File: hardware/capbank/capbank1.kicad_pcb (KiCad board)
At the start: 2 copper layers, 99 x 70.5 mm, 116 parts, among them J1 Screws, J3 Conn_01x02, J4 Conn_01x02, J5 Conn_01x06, K1 3570.1333.121 COMUS, K2 3570.1333.121 COMUS, K4 3570.1333.121 COMUS, SW2 SW_SPST, U1 ULN2003, U10 TS861IL, U11 NXJ1S1212MC, U12 LM317AEMP, U13 74HC14, U14 MCP1415, U15 MCP1415, U16 LM78L05ACZ, U2 OPA2202IDR, U3 MCP1525-TO, U4 MCP4921-EP, U5 PAI130M61, U6 ATtiny84A-P, U7 4046, U9 LM78L05ACZ, Y1 16MHz

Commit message: Small hardware changes
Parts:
- removed C18: 100n, PCM_Capacitor_SMD_AKL:C_0603_1608Metric
- removed C26, C49: 10u, PCM_Capacitor_THT_AKL:CP_Radial_D5.0mm_P2.00mm
- removed TP1, TP10, TP2, TP3, TP4, TP9: ~, TestPoint:TestPoint_THTPad_1.5x1.5mm_Drill0.7mm
- removed U6: ATtiny84A-P, Package_DIP:DIP-14_W7.62mm
- added C1: 100n, PCM_Capacitor_SMD_AKL:C_0603_1608Metric, F.Cu at (101.0, 100.0)
- added U8: ATtiny84A-SS, Package_SO:SOIC-14_3.9x8.7mm_P1.27mm, F.Cu at (131.5, 58.3)
- D4, D5, D6: value 1N5711 -> BAT46WJ; footprint Diode_THT:D_DO-35_SOD27_P7.62mm_Horizontal -> PCM_Diode_SMD_AKL:D_SOD-323
- D7: value 1N4007 -> 1N4007W; footprint Diode_THT:D_DO-35_SOD27_P7.62mm_Horizontal -> PCM_Diode_SMD_AKL:D_SOD-123
- U7: value 4046 -> 74HC4046AD; footprint Package_DIP:DIP-16_W7.62mm -> Package_SO:SOIC-16_3.9x9.9mm_P1.27mm
- Y1: footprint Crystal:Resonator-3Pin_W7.0mm_H2.5mm -> PCM_Crystal_Handsoldering_AKL:Resonator_SMD_muRata_CSTxExxV-3Pin_3.0x1.1mm_BigPads
- moved JP8 47.5 mm to (131.4, 52.4)
- moved C41 40.9 mm to (128.7, 70.2), turned to -90 degrees
- moved C46 40.5 mm to (115.5, 100.4)
- moved C48 40.1 mm to (102.7, 74.7), turned to 180 degrees
- moved D4 39.3 mm to (126.1, 107.4), turned to 90 degrees
- moved D5 39.2 mm to (125.3, 104.3)
- moved D6 39.1 mm to (126.1, 101.4), turned to -90 degrees
- moved C13 39.0 mm to (114.0, 92.2), turned to -90 degrees
- moved J4 38.2 mm to (116.6, 66.5)
- moved R16 38.1 mm to (127.0, 70.2), turned to 90 degrees
- moved C45 37.9 mm to (133.5, 98.8), turned to 0 degrees
- moved C20 37.8 mm to (117.0, 100.4), turned to -90 degrees
- moved H1 37.4 mm to (162.0, 92.0)
- moved C19 36.3 mm to (116.9, 106.3)
- moved C47 36.3 mm to (115.4, 106.3)
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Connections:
- J1 pad 1: GND -> V_SUPPLY
- J1 pad 2: V_SUPPLY -> GND
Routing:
- net V_SUPPLY: track 213.2 -> 167.4 mm, vias 3 -> 1
- net /Isolated/VTUNE: track 15.8 -> 61.4 mm, vias 0 -> 2
- net VDD: track 201.5 -> 156.9 mm, vias 4 -> 0
- net GND_ISOL: track 100.1 -> 140.6 mm, vias 17 -> 31
- net /Microcontroller/HVSP_CLK_FSK_IN: track 48.4 -> 9.27 mm, vias 6 -> 0
- net /Microcontroller/PRG_MOSI_I2C_SDA: track 39.5 -> 4.67 mm
- net /Microcontroller/FSK_DEMOD: track 4.53 -> 35.9 mm, vias 0 -> 4
- net /SCK: track 17.1 -> 38.2 mm, vias 0 -> 2
- net /Microcontroller/~{RESET}: track 31.4 -> 10.7 mm
- net /SDI: track 16.6 -> 34.9 mm
- net /Microcontroller/PRG_SCK_I2C_SCL: track 25.3 -> 7.00 mm
- net VDD_ISOL: track 84.5 -> 100.0 mm, vias 2 -> 1
- net HV_CLEAN: track 52.6 -> 67.9 mm, vias 2 -> 1
- net /Microcontroller/FSK Demod/FSK_DEMOD: track 5.53 -> 20.4 mm, vias 0 -> 2
- net V_SUPPLY_ISOL: track 28.9 -> 39.7 mm
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- added copper zone on F.Cu, net /Isolated/ANT1
- added copper zone on F.Cu, net /Isolated/ANT2
- added copper zone on F.Cu, net GND
- added copper zone on F.Cu, net GND_ISOL
- added copper zone on F.Cu, net Net-(D1-K)
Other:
- board size 99 x 70.5 mm -> 91 x 64 mm
- board text added: "+"
- board text added: "GND"
- board text added: "MISO"
- board text added: "MOSI"
- board text added: "SCK"
- board text added: "VDD"
- board text added: "Varactor Board Rev A"
- board text added: "contact@tatjam.eu"
- board text added: "~{RST}"
- board text added: "▲"

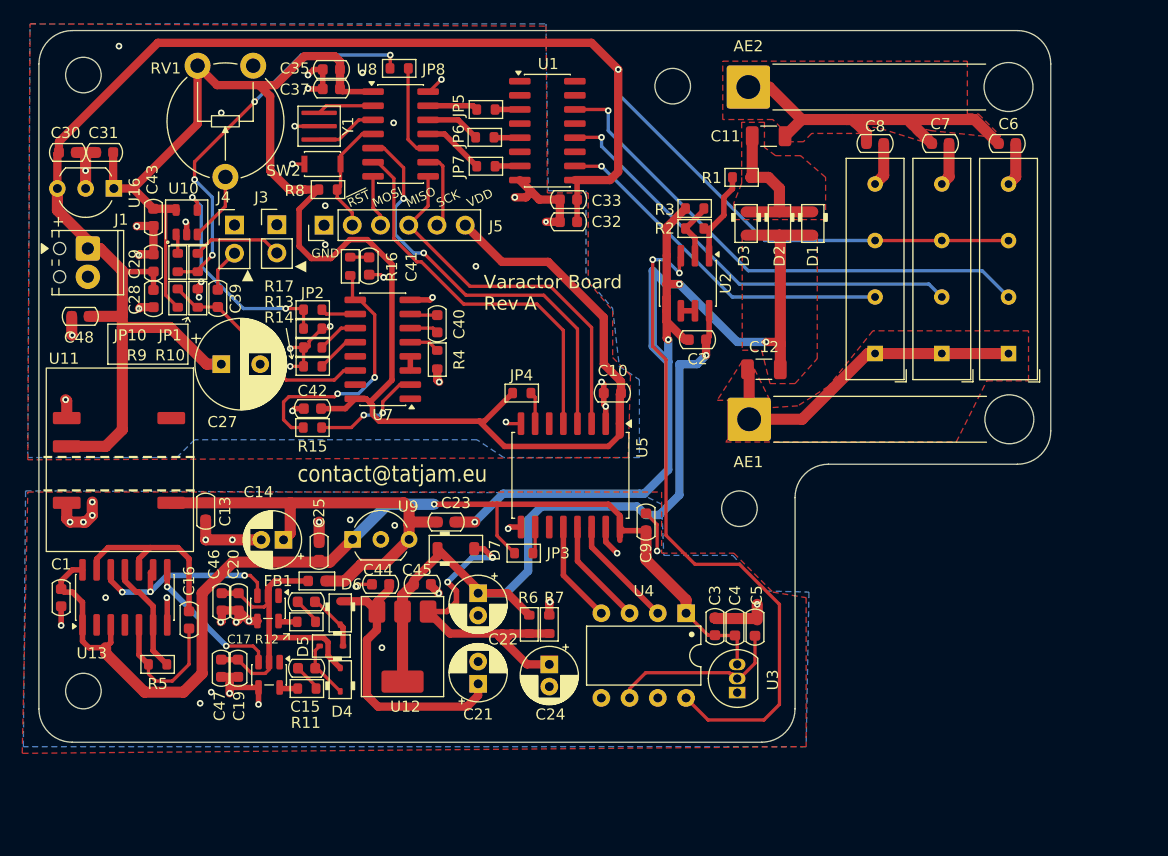
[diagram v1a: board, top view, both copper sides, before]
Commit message: Add footprint for buffered-filter and replace pot with digital pot
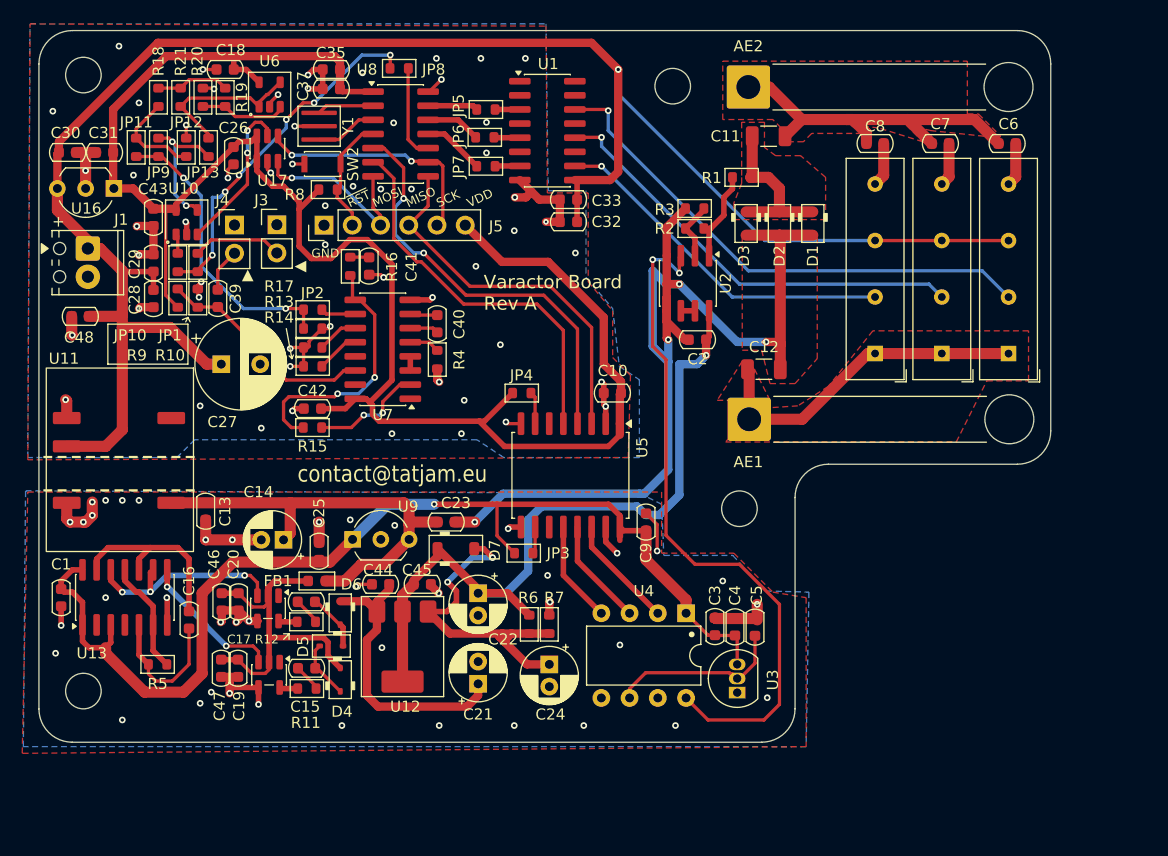
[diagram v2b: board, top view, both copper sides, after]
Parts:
- removed RV1: 10k, PCM_Potentiometer_THT_AKL:Potentiometer_Piher_PT-10-V10_Vertical
- added C18: 100n, PCM_Capacitor_SMD_AKL:C_0603_1608Metric, F.Cu at (115.8, 52.5)
- added C26: 100n, PCM_Capacitor_SMD_AKL:C_0603_1608Metric, F.Cu at (116.5, 60.2)
- added JP11: 0, PCM_Resistor_SMD_AKL:R_0603_1608Metric, F.Cu at (107.8, 59.5)
- added JP12: 0, PCM_Resistor_SMD_AKL:R_0603_1608Metric, F.Cu at (112.2, 59.5)
- added JP13: 0, PCM_Resistor_SMD_AKL:R_0603_1608Metric, F.Cu at (114.2, 59.5)
- added JP9: 0, PCM_Resistor_SMD_AKL:R_0603_1608Metric, F.Cu at (109.8, 59.5)
- added R18: 10k, PCM_Resistor_SMD_AKL:R_0603_1608Metric, F.Cu at (109.8, 55.0)
- added R19: 10k, PCM_Resistor_SMD_AKL:R_0603_1608Metric, F.Cu at (115.8, 55.0)
- added R20: 10k, PCM_Resistor_SMD_AKL:R_0603_1608Metric, F.Cu at (113.8, 55.0)
- added R21: 10k, PCM_Resistor_SMD_AKL:R_0603_1608Metric, F.Cu at (111.8, 55.0)
- added U17: MCP4012-xxxxCH, Package_TO_SOT_SMD:SOT-23-6, F.Cu at (119.5, 59.6)
- added U6: MCP6021T-E-OT, PCM_Package_TO_SOT_SMD_AKL:SOT-23-5, F.Cu at (119.8, 54.8)
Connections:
- net /Microcontroller/PRG_MOSI_I2C_SDA renamed /Microcontroller/PRG_MOSI_RHEO_UD
- net /Microcontroller/PRG_SCK_I2C_SCL renamed /Microcontroller/PRG_SCK_RHEO_CS
- net Net-(D4-A) renamed /BiasSupply/SWITCH_SUPPLY
- net Net-(U2A--) renamed /Isolated/Varactor/VBIAS_FB
- U10 pad 4: /Microcontroller/FSK Demod/FSK_DEMOD -> /Microcontroller/FSK Demod/FSK_FILT
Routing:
- net /Microcontroller/PRG_SCK_RHEO_CS: track 7.00 -> 21.8 mm, vias 0 -> 2
- net Net-(JP13-A): track 0.00 -> 14.6 mm
- net /Microcontroller/FSK Demod/FSK_FILT: track 0.00 -> 12.6 mm, vias 0 -> 2
- net /Microcontroller/PRG_MOSI_RHEO_UD: track 4.67 -> 17.0 mm, vias 0 -> 1
- net Net-(JP11-B): track 0.00 -> 8.86 mm
- net VDD: track 156.9 -> 165.0 mm
- net Net-(U10-+): track 6.22 -> 14.2 mm, vias 0 -> 2
- net Net-(U6-+): track 0.00 -> 7.87 mm
- net GND: track 55.5 -> 63.0 mm, vias 33 -> 57
- net Net-(R18-Pad2): track 0.00 -> 6.62 mm
- net /Microcontroller/FSK Demod/FSK_DEMOD: track 20.4 -> 26.2 mm
- net /Microcontroller/FSK_DEMOD: track 35.9 -> 32.1 mm, vias 4 -> 6
- net GND_ISOL: vias 31 -> 45

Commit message: Update PCB with learned lessons
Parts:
- added C34: 100n, PCM_Capacitor_SMD_AKL:C_0603_1608Metric, F.Cu at (123.5, 86.5)
- added JP14: 0, PCM_Resistor_SMD_AKL:R_0603_1608Metric, F.Cu at (140.0, 79.5)
- added JP15: 0, PCM_Resistor_SMD_AKL:R_0603_1608Metric, F.Cu at (139.9, 77.5)
- added JP16: 0, PCM_Resistor_SMD_AKL:R_0603_1608Metric, F.Cu at (140.0, 75.5)
- added R22: 1M, PCM_Resistor_SMD_AKL:R_0603_1608Metric, F.Cu at (158.8, 62.2)
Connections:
- net Net-(U7-VCOin) renamed /Microcontroller/FSK Demod/VCO_IN
- R1 pad 1: /Isolated/Varactor/VBIAS -> Net-(R1-Pad1)
- R15 pad 1: Net-(U7-PC1) -> /Microcontroller/FSK Demod/PC
- U7 pad 13: unconnected-(U7-PC2-Pad13) -> Net-(JP15-A)
- U7 pad 15: unconnected-(U7-ZOUT-Pad15) -> Net-(JP14-A)
- U7 pad 2: Net-(U7-PC1) -> Net-(JP16-A)
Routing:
- net /Microcontroller/FSK Demod/PC: track 0.00 -> 24.9 mm, vias 0 -> 2
- net Net-(JP14-A): track 0.00 -> 20.4 mm, vias 0 -> 2
- net Net-(JP15-A): track 0.00 -> 16.2 mm, vias 0 -> 2
- net Net-(JP16-A): track 0.00 -> 14.9 mm, vias 0 -> 2
- net Net-(U7-PC1): track 10.2 -> 0.00 mm, vias 2 -> 0
- net /Microcontroller/FSK Demod/VCO_IN: track 23.1 -> 25.5 mm
- net /Isolated/Varactor/VBIAS: track 8.52 -> 10.3 mm
- net Net-(R1-Pad1): track 0.00 -> 1.40 mm

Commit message: Some advances in pre-fabrication review
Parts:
- removed C14: 10u, PCM_Capacitor_THT_AKL:CP_Radial_D5.0mm_P2.00mm
- added FB2: 82223C (22uH), proj_footprints:82223C, F.Cu at (115.2, 91.7)
- added R23: 7k, PCM_Resistor_SMD_AKL:R_1812_4532Metric, B.Cu at (144.8, 97.5)
- added R24: 1.2k, PCM_Resistor_SMD_AKL:R_1206_3216Metric_Pad1.30x1.75mm_HandSolder, F.Cu at (123.2, 92.0)
- C13: value 100n -> 4.7u; footprint PCM_Capacitor_SMD_AKL:C_0603_1608Metric -> Capacitor_SMD:C_1210_3225Metric_Pad1.33x2.70mm_HandSolder
- C23, C30: value 100n -> 0.22u
- R7: footprint PCM_Resistor_SMD_AKL:R_0603_1608Metric -> PCM_Resistor_SMD_AKL:R_1210_3225Metric_Pad1.30x2.65mm_HandSolder; moved to B.Cu
- moved C13 5.09 mm to (119.0, 93.2)
- moved R6 1.66 mm to (144.5, 101.5)
- moved R7 0.91 mm to (144.8, 101.5), turned to 0 degrees
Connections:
- U11 pad 8: V_SUPPLY_ISOL -> Net-(U11-+VOUT)
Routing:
- net HV_CLEAN: track 67.9 -> 75.8 mm, vias 1 -> 2
- net GND_ISOL: track 140.6 -> 132.7 mm, vias 45 -> 46
- net V_SUPPLY_ISOL: track 39.7 -> 33.2 mm
- net Net-(U11-+VOUT): track 0.00 -> 4.38 mm
- net Net-(JP16-A): track 14.9 -> 10.8 mm
- net Net-(D7-A): track 30.6 -> 33.8 mm, vias 2 -> 3

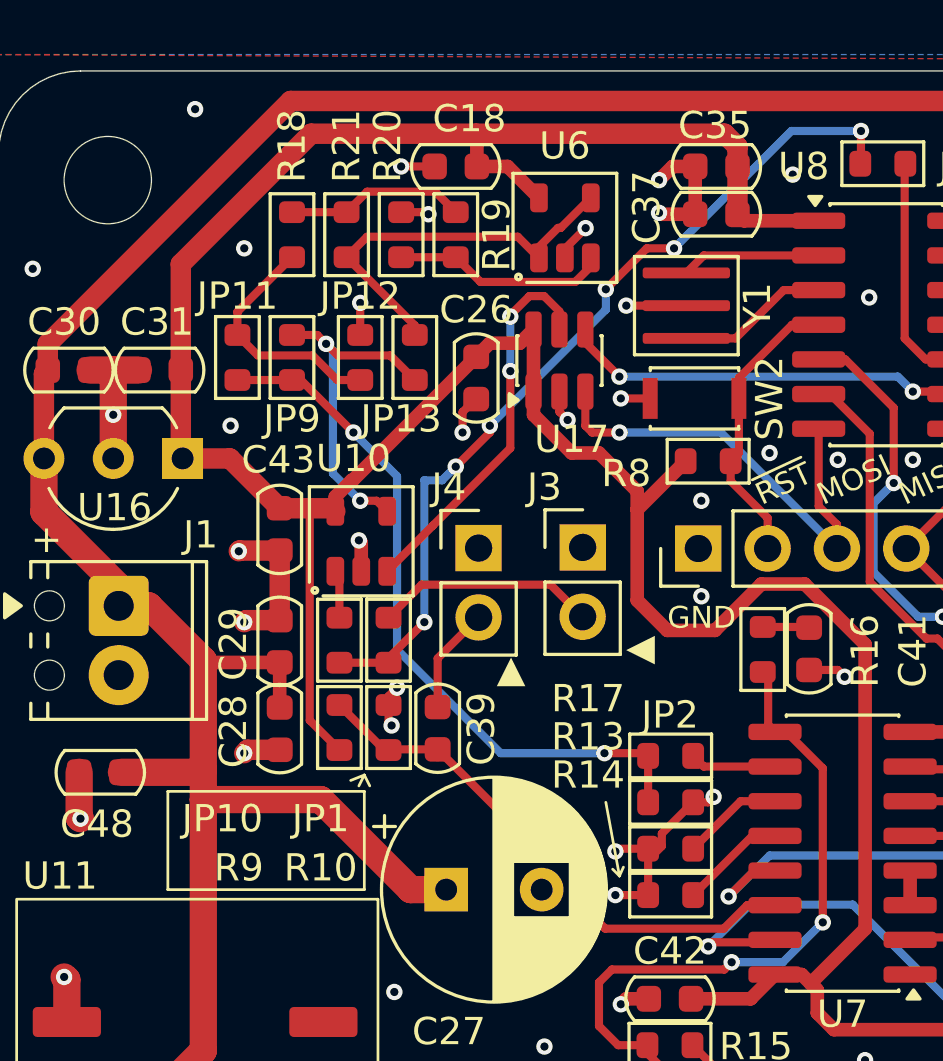
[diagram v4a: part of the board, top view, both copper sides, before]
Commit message: Add hysteresis to comparator
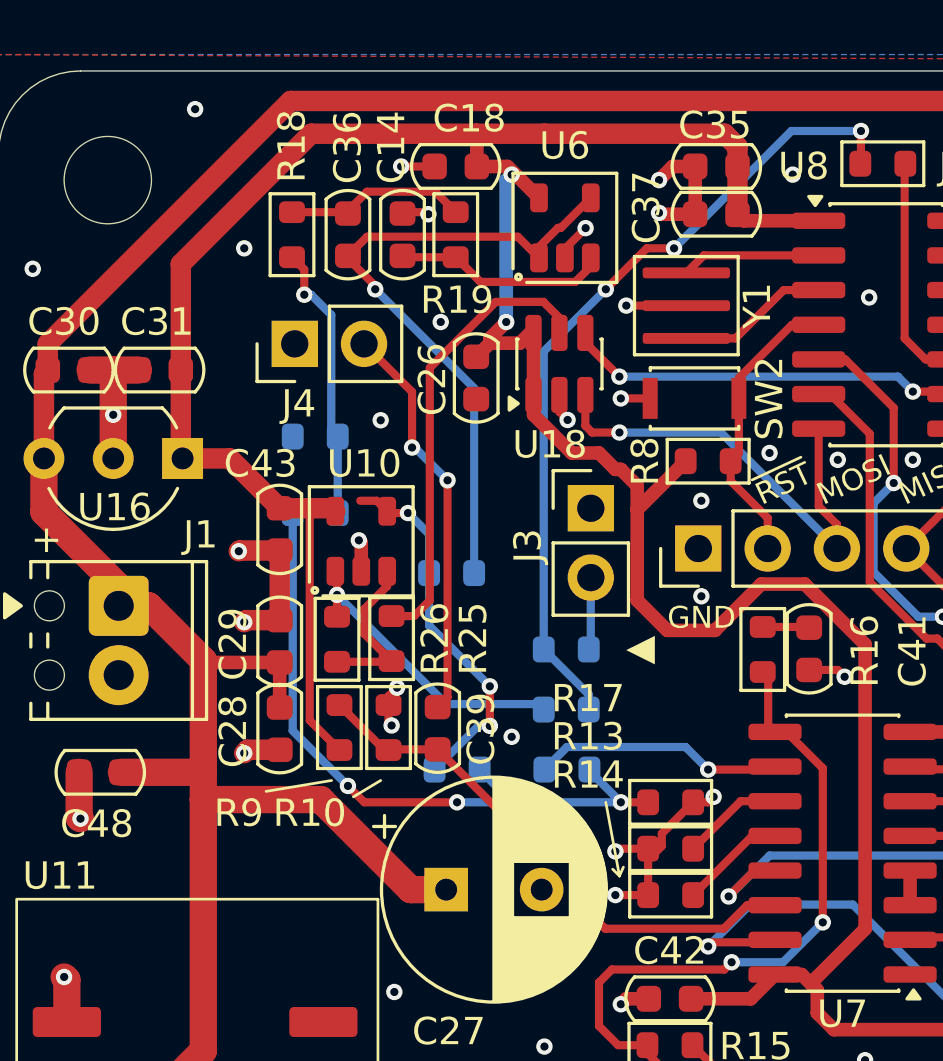
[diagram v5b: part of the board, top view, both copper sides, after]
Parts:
- removed R20, R21: 10k, PCM_Resistor_SMD_AKL:R_0603_1608Metric
- removed U17: MCP4012-xxxxCH, Package_TO_SOT_SMD:SOT-23-6
- added C14: 1n, PCM_Capacitor_SMD_AKL:C_0603_1608Metric, F.Cu at (113.8, 55.0)
- added C36: 1n, PCM_Capacitor_SMD_AKL:C_0603_1608Metric, F.Cu at (111.8, 55.0)
- added R25: 10k, PCM_Resistor_SMD_AKL:R_0603_1608Metric, F.Cu at (113.4, 69.8)
- added R26: 200k, PCM_Resistor_SMD_AKL:R_0603_1608Metric, F.Cu at (111.4, 69.8)
- added U18: MCP4013-xxxxCH, Package_TO_SOT_SMD:SOT-23-6, F.Cu at (119.5, 59.7)
- C34: value 100n -> 1n
- C41: value C -> 100n
- JP1, JP10, JP11, JP12, JP13, JP2, JP9: moved to B.Cu
- R15: value 10k -> 285k
- moved JP9 16.3 mm to (115.8, 74.6), turned to 180 degrees
- moved J4 10.1 mm to (109.8, 59.0), turned to 90 degrees
- moved JP10 8.69 mm to (119.8, 72.4), turned to 0 degrees
- moved JP13 8.01 mm to (115.6, 67.4), turned to 180 degrees
- moved JP1 6.52 mm to (119.8, 70.2), turned to 180 degrees
- moved JP11 6.37 mm to (110.6, 65.2), turned to 0 degrees
- moved JP2 3.83 mm to (119.8, 74.6), turned to 0 degrees
- moved JP12 3.34 mm to (110.6, 62.4), turned to 0 degrees
- moved J3 1.47 mm to (120.7, 65.0)
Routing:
- net Net-(U18-W): track 0.00 -> 16.7 mm
- net Net-(J4-Pin_2): track 3.91 -> 14.8 mm, vias 0 -> 2
- net Net-(JP13-A): track 14.6 -> 24.2 mm, vias 0 -> 1
- net /Microcontroller/FSK Demod/FSK_CMP: track 1.76 -> 11.2 mm, vias 0 -> 1
- net Net-(U10-+): track 14.2 -> 6.06 mm, vias 2 -> 0
- net Net-(JP2-A): track 3.16 -> 9.18 mm, vias 0 -> 1
- net Net-(J3-Pin_2): track 8.10 -> 2.67 mm
- net GND: track 63.0 -> 60.4 mm
- net /Microcontroller/FSK_DEMOD: track 32.1 -> 30.0 mm, vias 6 -> 3
- net Net-(JP11-B): track 8.86 -> 10.2 mm, vias 0 -> 1
- net VDD: track 165.0 -> 163.8 mm, vias 0 -> 2
- net /Microcontroller/FSK Demod/FSK_FILT: track 12.6 -> 13.7 mm, vias 2 -> 3
- net /Microcontroller/FSK Demod/FSK_DEMOD: track 26.2 -> 25.5 mm, vias 2 -> 3

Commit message: Various wiring fixes and add bleed resistor to antenna
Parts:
- added R20: 22M, PCM_Resistor_SMD_AKL:R_0603_1608Metric, F.Cu at (159.4, 82.5)
- added R27: 22M, PCM_Resistor_SMD_AKL:R_0603_1608Metric, F.Cu at (159.4, 85.7)
- added R28: 22M, PCM_Resistor_SMD_AKL:R_0603_1608Metric, F.Cu at (158.6, 88.0)
- added R29: 22M, PCM_Resistor_SMD_AKL:R_0603_1608Metric, F.Cu at (159.0, 58.4)
- added R30: 22M, PCM_Resistor_SMD_AKL:R_0603_1608Metric, F.Cu at (155.9, 59.5)
- added R31: 22M, PCM_Resistor_SMD_AKL:R_0603_1608Metric, F.Cu at (154.9, 62.1)
- C2, C45: value 100n -> 100n (@32V)
- C22: value 10u -> 10u (@32V)
- C36: value 1n -> 2n
- R18, R19: value 10k -> 1.7k
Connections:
- net /Microcontroller/HVSP_CLK_FSK_IN renamed /Microcontroller/FSK_IN
- J5 pad 3: /Microcontroller/PRG_MOSI_RHEO_UD -> /SDI
- J5 pad 5: /Microcontroller/PRG_SCK_RHEO_CS -> /SCK
- JP5 pad 1: /Microcontroller/HVSP_SDI_RELAY1 -> /Microcontroller/RELAY1
- JP5 pad 2: /Microcontroller/RELAY1 -> /Microcontroller/ORELAY1
- JP6 pad 1: /Microcontroller/HVSP_SII_RELAY2 -> /Microcontroller/RELAY2
- JP6 pad 2: /Microcontroller/RELAY2 -> /Microcontroller/ORELAY2
- JP7 pad 1: /Microcontroller/HVSP_SDO_RELAY3 -> /Microcontroller/RELAY3
- JP7 pad 2: /Microcontroller/RELAY3 -> /Microcontroller/ORELAY3
- U1 pad 1: unconnected-(U1-I1-Pad1) -> GND
- U1 pad 2: unconnected-(U1-I2-Pad2) -> GND
- U1 pad 3: /Microcontroller/RELAY1 -> /Microcontroller/ORELAY1
- U1 pad 4: unconnected-(U1-I4-Pad4) -> GND
- U1 pad 5: /Microcontroller/RELAY2 -> /Microcontroller/ORELAY2
- U1 pad 6: unconnected-(U1-I6-Pad6) -> GND
- U1 pad 7: /Microcontroller/RELAY3 -> /Microcontroller/ORELAY3
- U18 pad 3: /Microcontroller/PRG_MOSI_RHEO_UD -> /Microcontroller/RHEO_UD
- U18 pad 4: /Microcontroller/PRG_SCK_RHEO_CS -> /Microcontroller/RHEO_CS
- U8 pad 11: /Microcontroller/HVSP_SDO_RELAY3 -> /Microcontroller/RELAY3
- U8 pad 12: /Microcontroller/HVSP_SII_RELAY2 -> /Microcontroller/RELAY2
- U8 pad 13: /Microcontroller/HVSP_SDI_RELAY1 -> /Microcontroller/RELAY1
- U8 pad 5: /SCK -> /Microcontroller/RHEO_CS
- U8 pad 6: /SDI -> /Microcontroller/RHEO_UD
- U8 pad 7: /Microcontroller/PRG_MOSI_RHEO_UD -> /SDI
- U8 pad 9: /Microcontroller/PRG_SCK_RHEO_CS -> /SCK
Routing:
- net /Microcontroller/PRG_SCK_RHEO_CS: track 21.8 -> 0.00 mm, vias 2 -> 0
- net /Microcontroller/PRG_MOSI_RHEO_UD: track 17.0 -> 0.00 mm, vias 1 -> 0
- net /Microcontroller/RHEO_CS: track 0.00 -> 15.1 mm, vias 0 -> 2
- net GND: track 60.4 -> 75.1 mm, vias 57 -> 59
- net /Microcontroller/RHEO_UD: track 0.00 -> 9.58 mm, vias 0 -> 2
- net GND_ISOL: track 132.7 -> 138.7 mm, vias 46 -> 47
- net /SCK: track 38.2 -> 44.2 mm
- net /Microcontroller/HVSP_SDO_RELAY3: track 5.58 -> 0.00 mm
- net /Isolated/ANT2: track 33.0 -> 38.1 mm
- net /Microcontroller/HVSP_SII_RELAY2: track 4.93 -> 0.00 mm
- net /Microcontroller/HVSP_SDI_RELAY1: track 4.63 -> 0.00 mm
- net /Isolated/ANT1: track 30.3 -> 34.8 mm
- net /Microcontroller/RELAY3: track 2.24 -> 5.58 mm
- net /Microcontroller/RELAY2: track 2.34 -> 4.93 mm
- net /Microcontroller/RELAY1: track 2.23 -> 4.63 mm
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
